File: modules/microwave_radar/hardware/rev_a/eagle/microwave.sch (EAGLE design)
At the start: 50 parts, among them J1 MODULE_GENERIC, J2 TC2030-JLINK-L, U1 SAM4LC8AA, U2 TLV62130, U3 MSGEQ7, U4 HB100, U5 OP284E_SEPARATE

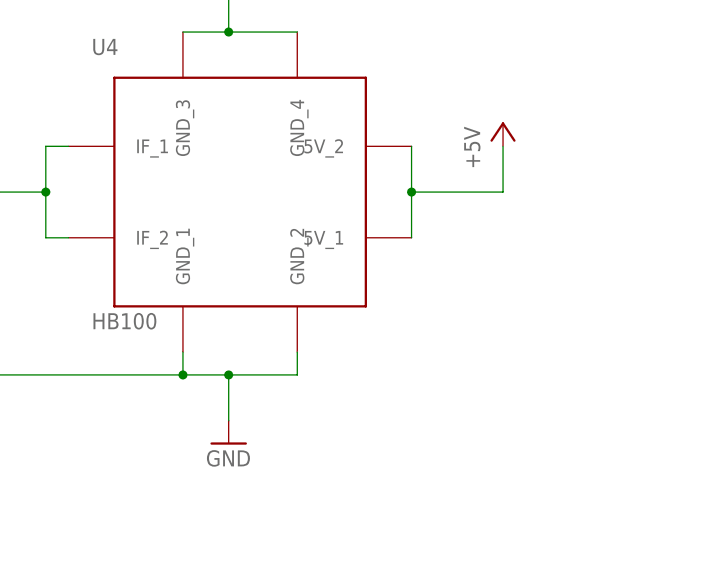
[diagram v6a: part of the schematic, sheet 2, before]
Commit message: Add holes and add cap on HB100
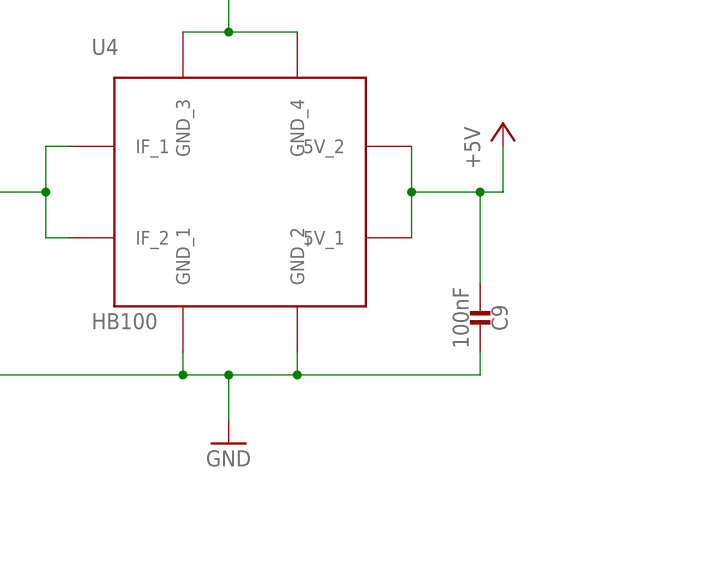
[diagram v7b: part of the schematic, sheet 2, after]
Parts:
- added C9: 100nF, passives:CAPACITOR0402_CAP
- U4: DIGIKEY (none) -> SAM1067-02-ND
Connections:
- net +5V: now also C9.2
- net GND: now also C9.1
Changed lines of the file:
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@@
 <part name="+3V3" library="supply1" deviceset="+3V3" device=""/>
 <part name="GND7" library="umich" deviceset="GND" device=""/>
-<part name="U4" library="microwave_radar" deviceset="HB100" device=""/>
+<part name="U4" library="microwave_radar" deviceset="HB100" device="">
+<attribute name="DIGIKEY" value="SAM1067-02-ND"/>
+</part>
 <part name="U5" library="microwave_radar" deviceset="OP284E_SEPARATE" device="">
 <attribute name="DIGIKEY" value="OP284ESZ-ND"/>
@@
 <part name="R16" library="passives" deviceset="RESISTOR" device="0603_RES" value="200k">
 <attribute name="DIGIKEY" value="RHM200KCFCT-ND"/>
+</part>
+<part name="C9" library="passives" deviceset="CAPACITOR" device="0402_CAP" value="100nF">
+<attribute name="DIGIKEY" value="490-10777-1-ND"/>
 </part>
 </parts>
@@
 <instance part="+3V3" gate="G$1" x="76.2" y="139.7"/>
 <instance part="GND7" gate="1" x="76.2" y="104.14"/>
-<instance part="U4" gate="G1" x="160.02" y="116.84"/>
+<instance part="U4" gate="G1" x="160.02" y="116.84">
+<attribute name="DIGIKEY" x="160.02" y="116.84" size="1.778" layer="96" display="off"/>
+</instance>
 <instance part="U5" gate="_A" x="60.96" y="43.18">
 <attribute name="DIGIKEY" x="60.96" y="43.18" size="1.778" layer="96" display="off"/>
@@
 <instance part="U5" gate="_B" x="119.38" y="45.72"/>
 <instance part="U5" gate="G$2" x="76.2" y="121.92"/>
+<instance part="C9" gate="G$1" x="185.42" y="101.6" rot="R180">
+<attribute name="DIGIKEY" x="185.42" y="101.6" size="1.778" layer="96" rot="R180" display="off"/>
+</instance>
 </instances>
 <busses>
@@
 <pinref part="U4" gate="G1" pin="GND_3"/>
 <pinref part="U4" gate="G1" pin="GND_4"/>
+<wire x1="165.1" y1="96.52" x2="185.42" y2="96.52" width="0.1524" layer="91"/>
+<junction x="165.1" y="96.52"/>
+<pinref part="C9" gate="G$1" pin="1"/>
+<wire x1="185.42" y1="96.52" x2="185.42" y2="99.06" width="0.1524" layer="91"/>
 </segment>
 <segment>
@@
 <wire x1="177.8" y1="121.92" x2="177.8" y2="116.84" width="0.1524" layer="91"/>
 <wire x1="177.8" y1="116.84" x2="177.8" y2="111.76" width="0.1524" layer="91"/>
-<wire x1="177.8" y1="116.84" x2="187.96" y2="116.84" width="0.1524" layer="91"/>
+<wire x1="177.8" y1="116.84" x2="185.42" y2="116.84" width="0.1524" layer="91"/>
 <junction x="177.8" y="116.84"/>
 <pinref part="P+2" gate="1" pin="+5V"/>
+<wire x1="185.42" y1="116.84" x2="187.96" y2="116.84" width="0.1524" layer="91"/>
 <wire x1="187.96" y1="116.84" x2="187.96" y2="121.92" width="0.1524" layer="91"/>
 <pinref part="U4" gate="G1" pin="5V_1"/>
 <pinref part="U4" gate="G1" pin="5V_2"/>
-</segment>
-</net>
+<pinref part="C9" gate="G$1" pin="2"/>
+<wire x1="185.42" y1="106.68" x2="185.42" y2="116.84" width="0.1524" layer="91"/>
+<junction x="185.42" y="116.84"/>
+</segment>
+</net>

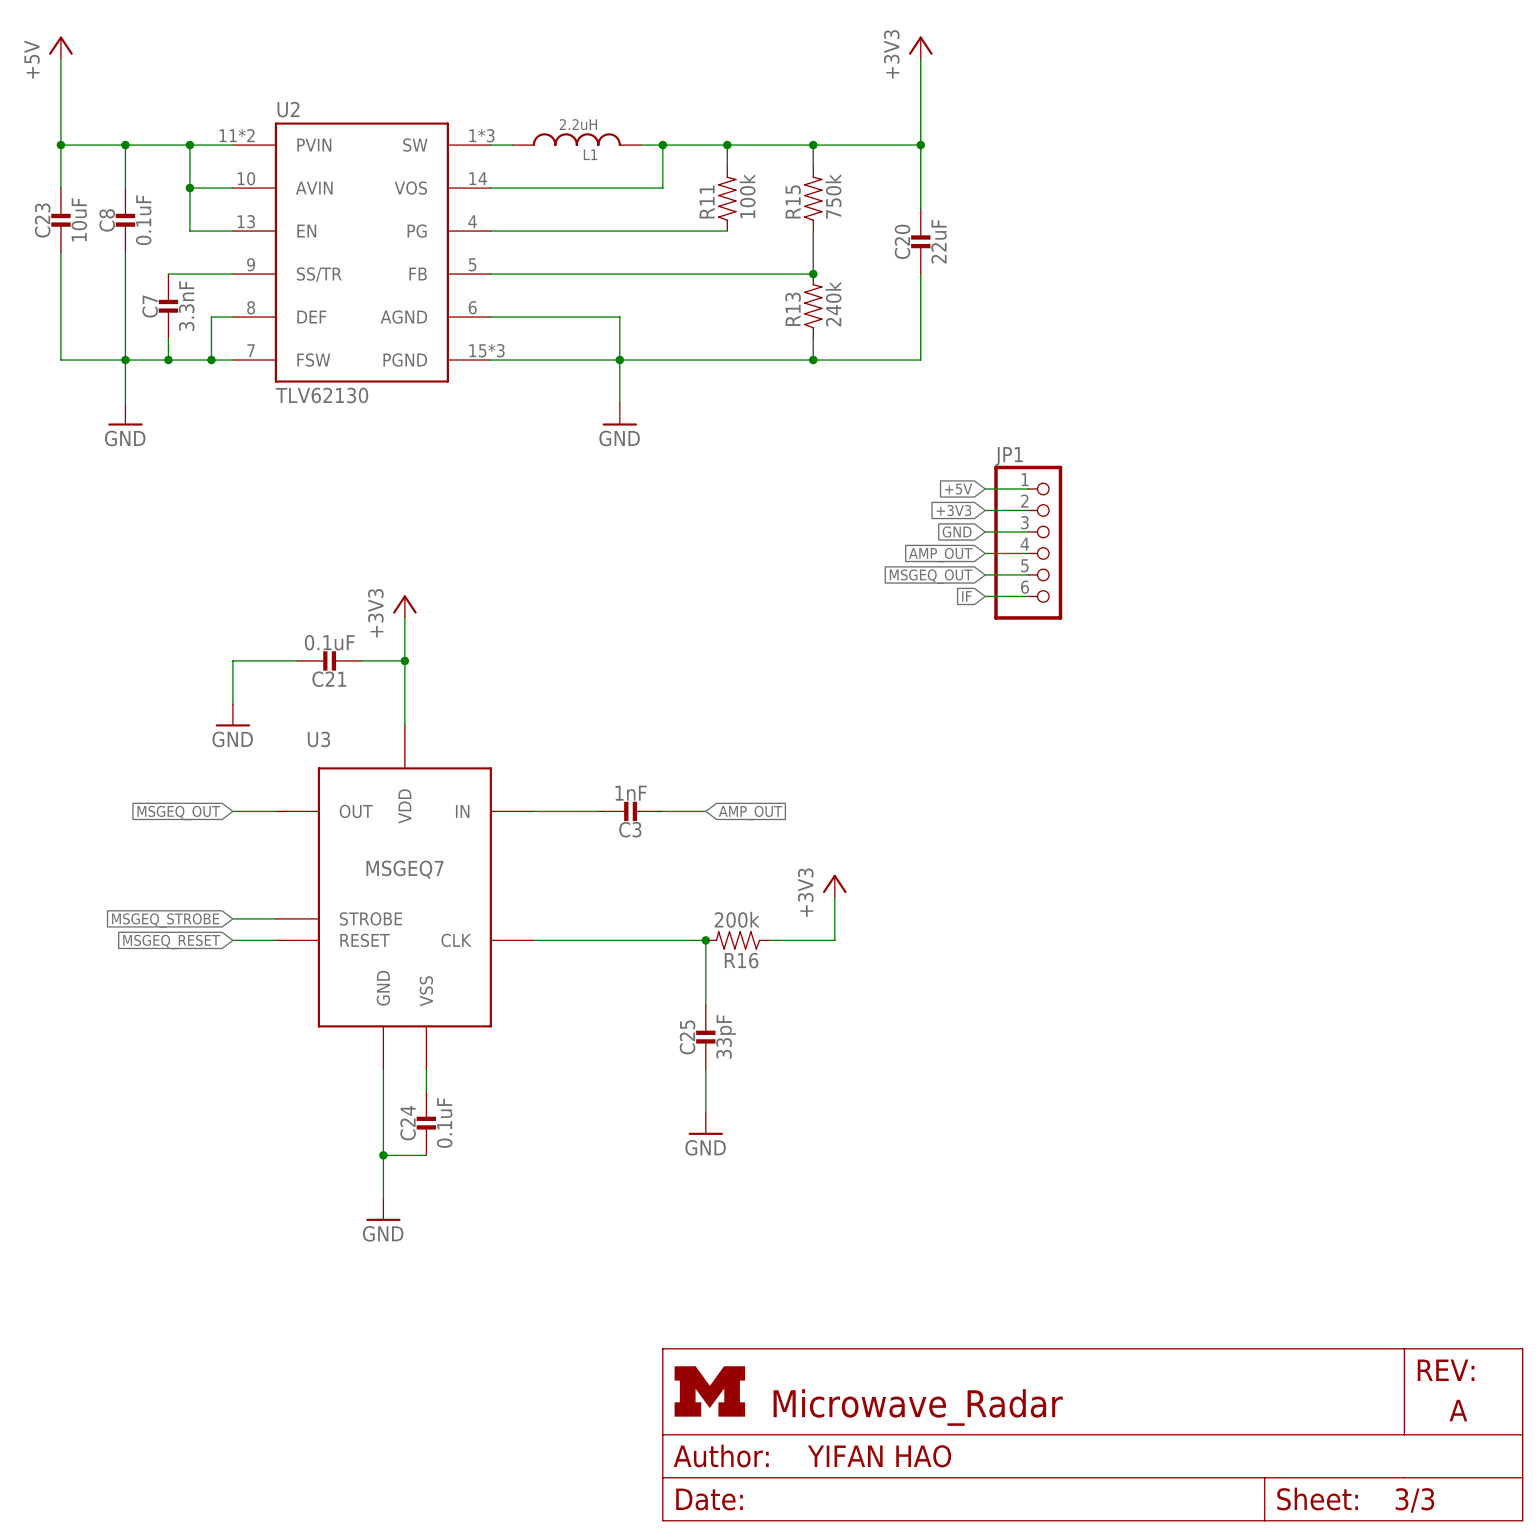
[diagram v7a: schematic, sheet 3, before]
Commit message: Run Pat's script after adding cap
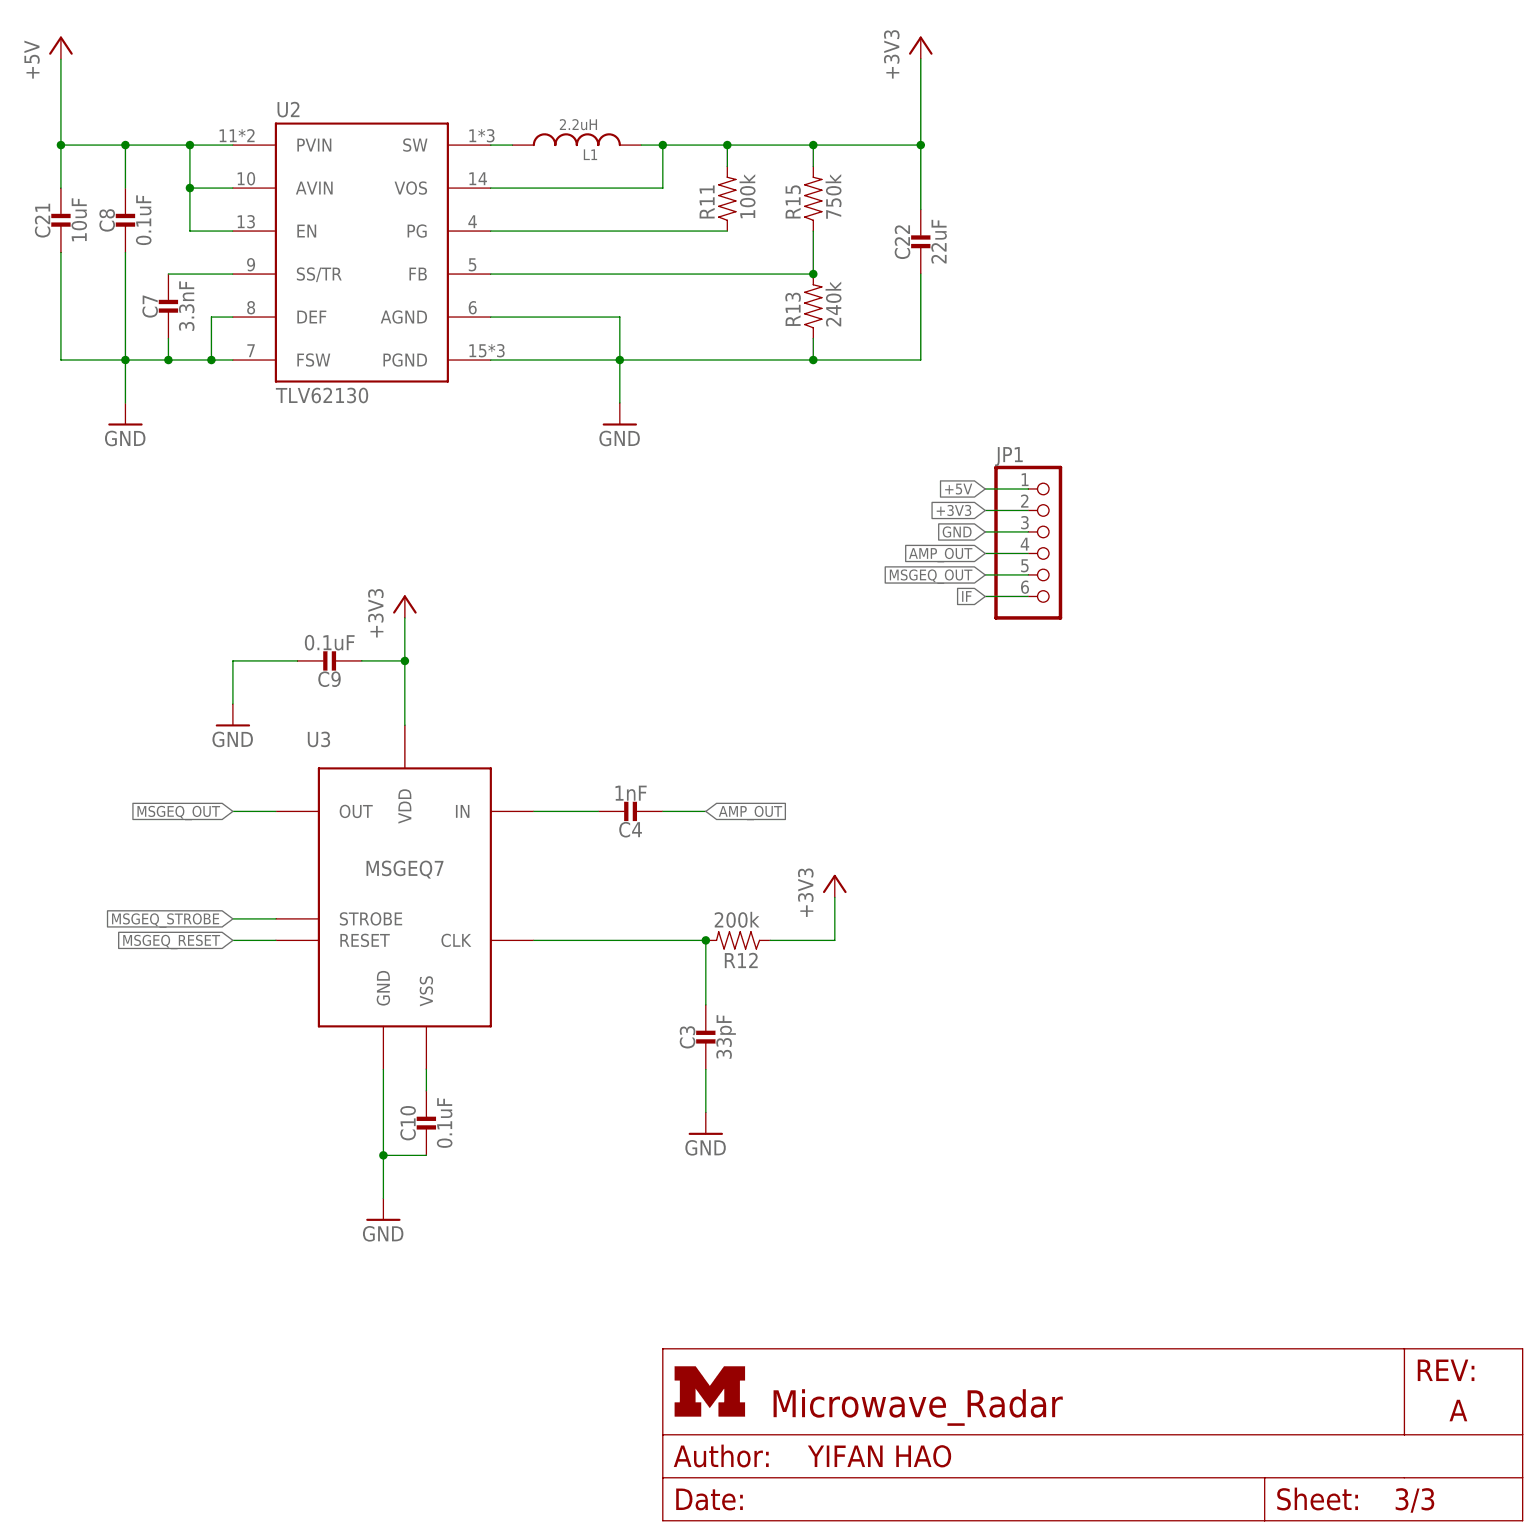
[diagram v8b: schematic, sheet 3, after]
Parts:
- removed C25: 33pF, passives:CAPACITOR0603_CAP
- added C4: 1nF, passives:CAPACITOR0603_CAP
- C17: value 4.7uF -> 100nF; DIGIKEY 1276-1481-1-ND -> 490-10777-1-ND
- C20: value 22uF -> 4.7uF; device passives:CAPACITOR0603_CAP -> passives:CAPACITOR0402_CAP; DIGIKEY 1276-1193-1-ND -> 1276-1481-1-ND
- C21: value 0.1uF -> 10uF; device passives:CAPACITOR0603_CAP -> passives:CAPACITOR0805_CAP; DIGIKEY 490-1532-1-ND -> 490-5523-1-ND
- C22: value 100uF -> 22uF; device passives:CAPACITOR1210_CAP -> passives:CAPACITOR0603_CAP; DIGIKEY 490-3390-1-ND -> 1276-1193-1-ND
- C23: value 10uF -> 100uF; device passives:CAPACITOR0805_CAP -> passives:CAPACITOR1210_CAP; DIGIKEY 490-5523-1-ND -> 490-3390-1-ND
- C3: value 1nF -> 33pF; DIGIKEY 490-1494-1-ND -> 490-1415-1-ND
- C9: value 100nF -> 0.1uF; device passives:CAPACITOR0402_CAP -> passives:CAPACITOR0603_CAP; DIGIKEY 490-10777-1-ND -> 490-1532-1-ND
- renumbered C24 to C10, R16 to R12
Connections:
- net +3V3: now also C22.1, C9.2; no longer C20.1, C21.2
- net +5V: now also C17.2, C21.1; no longer C23.1, C9.2
- net AMP_OUT: now also C4.2; no longer C3.2
- net GND: now also C17.1, C19.1, C21.2, C22.2, C23.1, C3.2; no longer C18.1, C20.2, C21.1, C22.1, C23.2, C25.2
- net IF: now also C18.1; no longer C17.1
- net N$1: now also C23.2; no longer C22.2
- net N$15: now also C19.2; no longer C18.2
- net N$17: now also C20.1; no longer C19.1
- net N$18: now also C20.2; no longer C19.2
- net N$2: now also C3.1; no longer C25.1
- net N$3: now also C4.1; no longer C3.1
- net N$9: now also C18.2; no longer C17.2
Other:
- moved on the sheet: C17, C18, C19, C21, C3
